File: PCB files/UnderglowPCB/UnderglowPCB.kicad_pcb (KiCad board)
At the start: 4 copper layers, 67 parts, among them J1 USB_B_Micro, J10 Screw_Terminal_01x03, J11 Screw_Terminal_01x03, J12 DB9_Male, J2 Screw_Terminal_01x03, J3 Screw_Terminal_01x03, J4 Conn_01x07, J5 Conn_01x05, J6 Screw_Terminal_01x03, J7 Screw_Terminal_01x03, J8 Screw_Terminal_01x03, J9 Screw_Terminal_01x03, Q1 S8050, Q2 S8050, SW1 SW_Push, U1 CP2102N-A01-GQFN28, U2 TPS62133, U3 74HC14, U4 74HC14, U5 LD56100DPU33R, U6 ESP32-WROOM-32D, U7 SN65HVD230, U8 USBLC6-2SC6

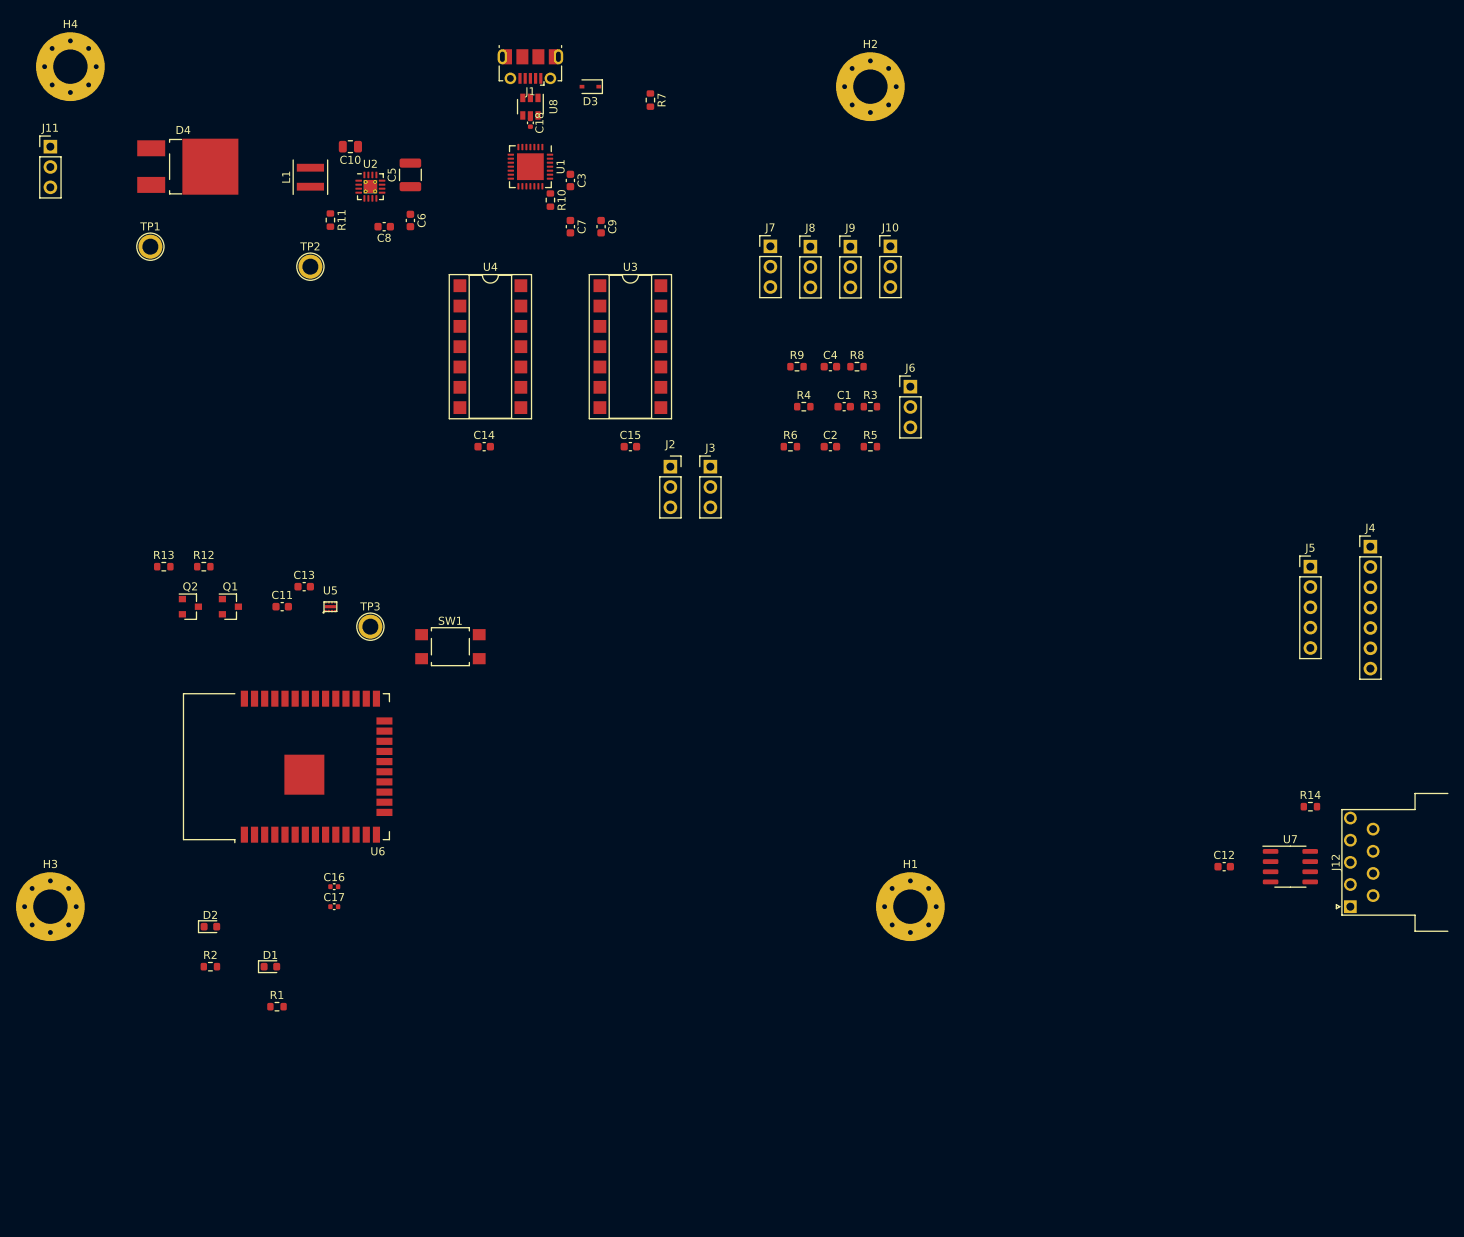
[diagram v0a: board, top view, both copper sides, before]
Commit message: Version 1.0.0 of PCB is almost done. Need tooling holes and holds for DB9 mount.
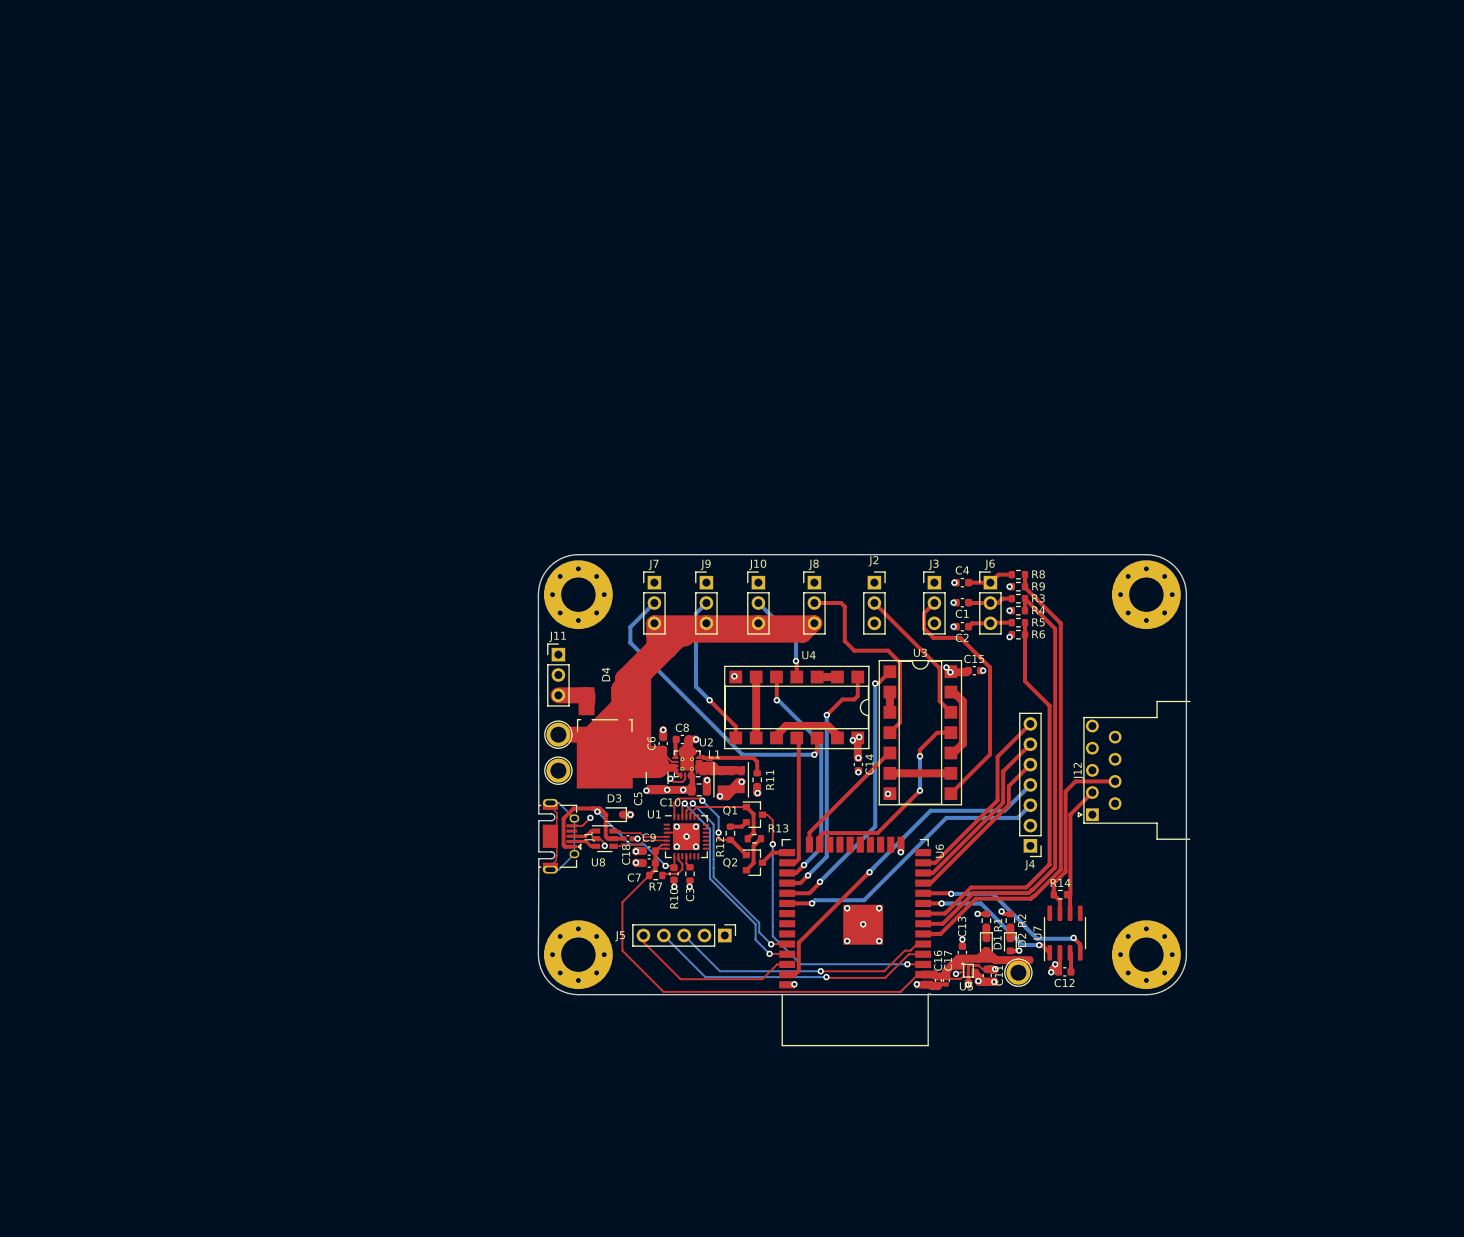
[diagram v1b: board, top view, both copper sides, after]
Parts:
- removed SW1: SW_Push, Button_Switch_SMD:SW_SPST_TL3305A
- J1: footprint Connector_USB:USB_Micro-B_Molex-105017-0001 -> Connector_USB:USB_Micro-AB_Molex_47590-0001
- moved R2 100.2 mm to (160.0, 126.8), turned to 90 degrees
- moved D2 100.0 mm to (160.0, 129.8), turned to 270 degrees
- moved C11 99.5 mm to (157.1, 133.6), turned to 90 degrees
- moved R7 96.9 mm to (115.7, 121.1), turned to 180 degrees
- moved J1 96.2 mm to (102.5, 116.2), turned to 270 degrees
- moved C13 94.1 mm to (154.0, 130.7), turned to 90 degrees
- moved U8 92.0 mm to (109.3, 116.5), turned to 0 degrees
- moved L1 91.9 mm to (125.1, 109.2), turned to 270 degrees
- moved TP3 91.8 mm to (161.0, 133.2), turned to 270 degrees
- moved U5 91.8 mm to (154.8, 133.0), turned to 270 degrees
- moved H4 91.6 mm to (106.0, 86.0)
- moved C10 91.5 mm to (121.1, 110.4), turned to 0 degrees
- moved D3 91.0 mm to (110.5, 113.5)
- moved C18 90.3 mm to (112.2, 116.5), turned to 0 degrees
- moved J11 89.8 mm to (103.5, 93.5)
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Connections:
- C5 pad 1: Net-(C5-Pad1) -> +12V
- C6 pad 1: Net-(C5-Pad1) -> +12V
- D4 pad 1: Net-(C5-Pad1) -> +12V
- D4 pad 2: +12V -> CAR_12V
- J11 pad 1: +12V -> GND
- J11 pad 3: GND -> CAR_12V
- J4 pad 2: +3V3 -> +5V
- U2 pad 10: Net-(C5-Pad1) -> +12V
- U2 pad 11: Net-(C5-Pad1) -> +12V
- U2 pad 12: Net-(C5-Pad1) -> +12V
- U2 pad 13: Net-(C5-Pad1) -> +12V
- U6 pad 10: UG_LOW_RIGHT -> CAN_RX
- U6 pad 11: UG_LOW_REAR -> OLED_RESET
- U6 pad 12: UG_LOW_FRONT -> OLED_DC
- U6 pad 13: UG_LOW_SPARE_1 -> OLED_CS
- U6 pad 14: RELAY_OUT -> Net-(U6-Pad14)
- U6 pad 16: UG_LOW_LEFT -> Net-(U6-Pad16)
- U6 pad 24: OLED_CS -> UG_LOW_SPARE_1
- U6 pad 26: OLED_DC -> UG_LOW_FRONT
- U6 pad 27: CAN_TX -> UG_LOW_REAR
- U6 pad 28: CAN_RX -> UG_LOW_RIGHT
- U6 pad 29: OLED_RESET -> UG_LOW_LEFT
- U6 pad 33: JOYSTICK_B -> Net-(U6-Pad33)
- U6 pad 36: Net-(SW1-Pad1) -> JOYSTICK_B
- U6 pad 4: Net-(U6-Pad4) -> JOYSTICK_Y
- U6 pad 5: BRAKE_LOW -> JOYSTICK_X
- U6 pad 6: TURN_RIGHT_LOW -> BRAKE_LOW
- U6 pad 7: TURN_LEFT_LOW -> TURN_RIGHT_LOW
- U6 pad 8: JOYSTICK_X -> TURN_LEFT_LOW
- U6 pad 9: JOYSTICK_Y -> CAN_TX
- U8 pad 1: USB_D- -> USB_D+
- U8 pad 3: USB_D+ -> USB_D-
- U8 pad 4: D+ -> D-
- U8 pad 6: D- -> D+
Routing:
- net +12V: track 0.00 -> 144.0 mm
- net +3V3: track 0.00 -> 89.7 mm
- net BRAKE_LOW: track 0.00 -> 59.3 mm
- net TURN_RIGHT_LOW: track 0.00 -> 56.1 mm
- net GND: track 0.00 -> 54.6 mm, vias 0 -> 42
- net TURN_LEFT_LOW: track 0.00 -> 51.4 mm
- net MOSI: track 0.00 -> 42.8 mm, vias 0 -> 1
- net UNDRGLW_FRNT: track 0.00 -> 37.2 mm, vias 0 -> 1
- net EN: track 0.00 -> 36.3 mm, vias 0 -> 2
- net JOYSTICK_Y: track 0.00 -> 35.8 mm, vias 0 -> 1
- net SPICLK: track 0.00 -> 35.5 mm, vias 0 -> 1
- net UG_LOW_LEFT: track 0.00 -> 34.9 mm, vias 0 -> 2
- net JOYSTICK_X: track 0.00 -> 33.1 mm, vias 0 -> 1
- net VBUS: track 0.00 -> 32.5 mm, vias 0 -> 2
- net 5V_LED_SPARE_2: track 0.00 -> 31.8 mm
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- added copper zone on In2.Cu, net +5V
- added copper zone on In1.Cu, net GND
- added copper zone on F.Cu, net Net-(L1-Pad1)
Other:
- board outline added: 81 x 55 mm
- net class Default: clearance 0.2 -> 0.1; trace_width 0.25 -> 0.4
- rule trace_clearance: 0.2 -> 0.1
- rule trace_min: 0.2 -> 0.15

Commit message: Minor PCB updates
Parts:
- added REF**: Pin_D1.0mm_L10.0mm, Connector_Pin:Pin_D1.0mm_L10.0mm, F.Cu at (109.8, 91.2)
- J12: footprint Connector_Dsub:DSUB-9_Male_Horizontal_P2.77x2.84mm_EdgePinOffset9.40mm -> UnderglowPCB:DB9
- moved J12 6.15 mm to (173.0, 108.0)
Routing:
- net GND: track 54.6 -> 74.8 mm
- net +5V: track 31.6 -> 40.8 mm
- net +3V3: track 89.7 -> 98.8 mm
- net Net-(J12-Pad7): track 22.9 -> 24.2 mm
- net Net-(J12-Pad2): track 16.8 -> 18.1 mm
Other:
- board text added: "+"
- board text added: "+3.3V"
- board text added: "+5V"
- board text added: "12V TEST POINT"
- board text added: "3.3V TEST POINT"
- board text added: "5V TEST POINT"
- board text added: "CAN BUS"
- board text added: "FRONT"
- board text added: "JOYSTICK"
- board text added: "LEFT"
- board text added: "REAR"
- board text added: "RIGHT"
- board text added: "SCREEN"
- board text added: "SPARE 1"
- board text added: "SPARE 2"
- board text added: "USB"

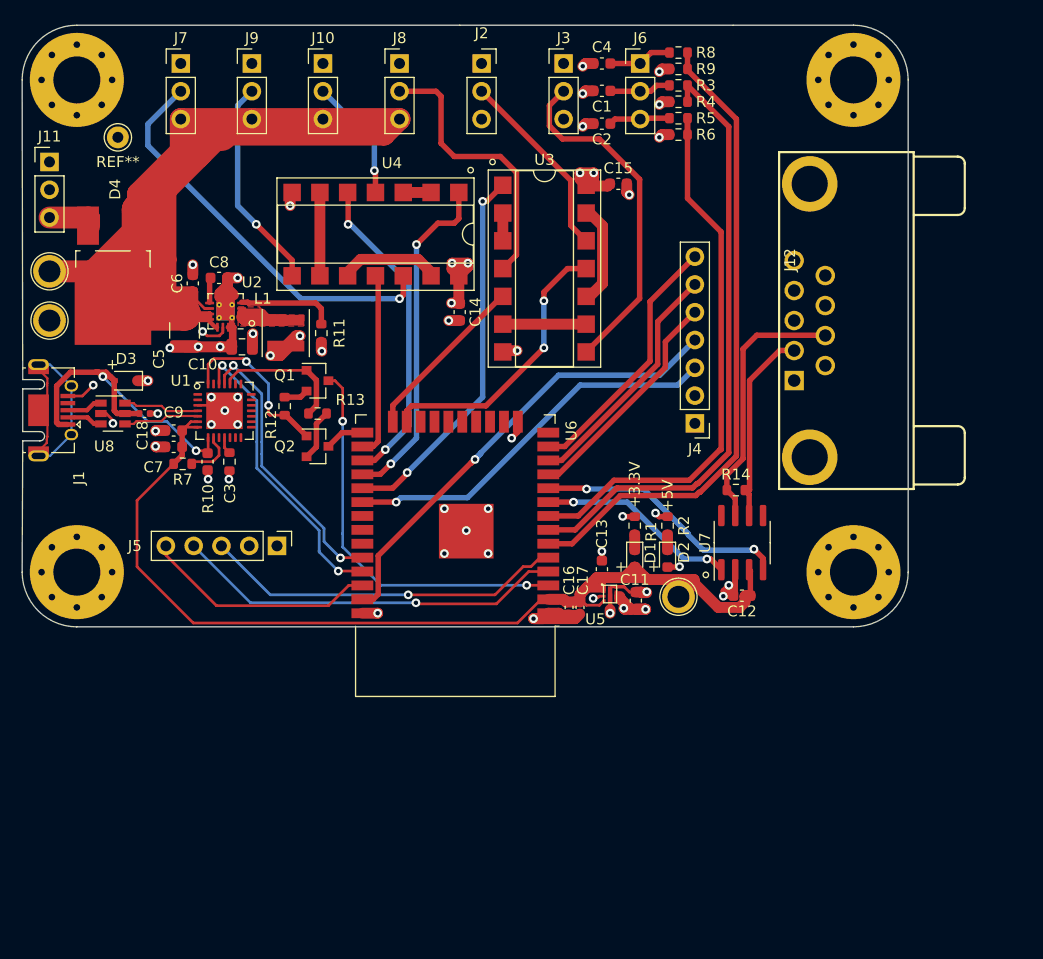
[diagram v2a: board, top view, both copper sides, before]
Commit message: Posted to reddit, changes include TVS Zener diodes and new power solution. That's a lot bigger.
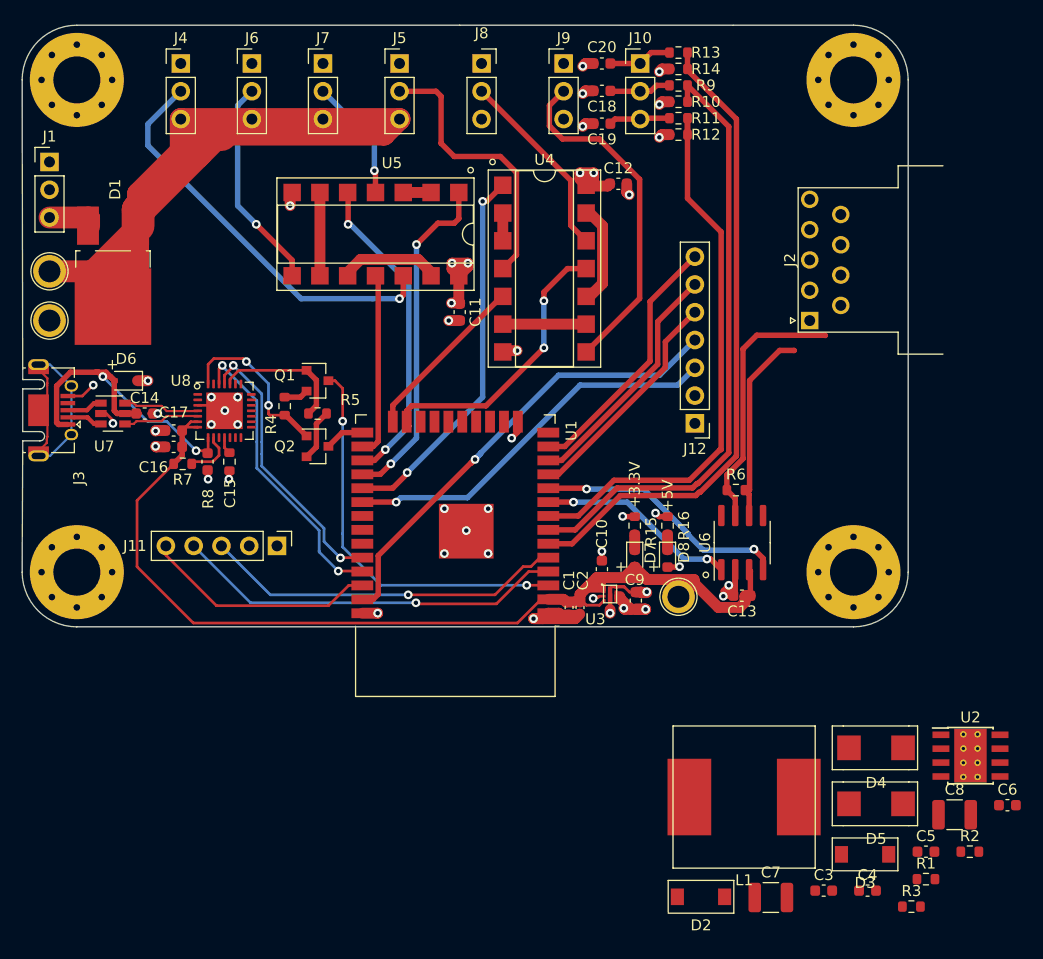
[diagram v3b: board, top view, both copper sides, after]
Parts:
- removed the C10 at (121.1, 110.4)
- removed the C18 at (112.2, 116.5)
- removed the J12 at (173.0, 108.0)
- removed the R11 at (128.3, 109.2)
- removed REF**: Pin_D1.0mm_L10.0mm, Connector_Pin:Pin_D1.0mm_L10.0mm
- added C14: .1u, Capacitor_SMD:C_0603_1608Metric, F.Cu at (112.2, 116.5)
- added C3: 2.2u, Capacitor_SMD:C_0603_1608Metric, F.Cu at (174.3, 160.1)
- added C4: 2.2u, Capacitor_SMD:C_0603_1608Metric, F.Cu at (178.3, 160.1)
- added C7: 47u, Capacitor_SMD:C_1210_3225Metric, F.Cu at (169.4, 160.7)
- added D2: TPSMA6L15A, UnderglowPCB:TPSMA6L15A, F.Cu at (163.1, 160.7)
- added D3: VSSAF512, UnderglowPCB:TPSMA6L15A, F.Cu at (178.1, 156.8)
- added D4: TPSMB15CA, UnderglowPCB:TPSMB15CA, F.Cu at (179.1, 147.1)
- added D5: TPSMB15CA, UnderglowPCB:TPSMB15CA, F.Cu at (179.1, 152.2)
- added J2: DB9_Male, Connector_Dsub:DSUB-9_Male_Horizontal_P2.77x2.84mm_EdgePinOffset9.40mm, F.Cu at (173.0, 108.0)
- added R1: 49.9k, Resistor_SMD:R_0603_1608Metric, F.Cu at (183.6, 159.1)
- added R2: 100k, Resistor_SMD:R_0603_1608Metric, F.Cu at (187.6, 156.6)
- added R3: 17.8k, Resistor_SMD:R_0603_1608Metric, F.Cu at (182.3, 161.6)
- C5: value 10u -> 22n; footprint Capacitor_SMD:C_1210_3225Metric -> Capacitor_SMD:C_0603_1608Metric
- C6: value 0.1u -> .1u
- C8: value 3.3n -> 47u; footprint Capacitor_SMD:C_0603_1608Metric -> Capacitor_SMD:C_1210_3225Metric
- L1: value 2.2u -> SRR1208-6R5ML; footprint Inductor_SMD:L_Coilcraft_XxL4020 -> UnderglowPCB:SRR1208
- U2: value TPS62133 -> LMR14030-Q1; footprint Package_DFN_QFN:VQFN-16-1EP_3x3mm_P0.5mm_EP1.68x1.68mm_ThermalVias -> Package_SO:Texas_HSOP-8-1EP_3.9x4.9mm_P1.27mm_ThermalVias
- moved C6 88.4 mm to (191.1, 152.3), turned to 0 degrees
- moved C8 83.2 mm to (186.2, 153.2)
- moved C5 82.9 mm to (183.6, 156.6), turned to 0 degrees
- moved U2 79.3 mm to (187.7, 147.8), turned to 0 degrees
- moved L1 59.6 mm to (167.0, 151.6), turned to 0 degrees
- renumbered C16 to C1, C13 to C10, C14 to C11, C15 to C12, C12 to C13, C3 to C15, C7 to C16, C9 to C17, C1 to C18, C2 to C19, C17 to C2, C4 to C20, C11 to C9, D4 to D1, D3 to D6, D1 to D7, D2 to D8, J11 to J1, J6 to J10, J5 to J11, J4 to J12, J1 to J3, J7 to J4, J8 to J5, J9 to J6, J10 to J7, J2 to J8, J3 to J9, R4 to R10, R5 to R11, R6 to R12, R8 to R13, R9 to R14, R1 to R15, R2 to R16, R12 to R4, R13 to R5, R14 to R6, R10 to R8, R3 to R9, U6 to U1, U5 to U3, U3 to U4, U4 to U5, U7 to U6, U8 to U7, U1 to U8
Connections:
- net RELAY_OUT renamed Net-(J1-Pad2)
- C5 pad 1: +12V -> Net-(C5-Pad1)
- C6 pad 1: +12V -> Net-(C6-Pad1)
- C6 pad 2: GND -> Net-(C6-Pad2)
- C8 pad 1: Net-(C8-Pad1) -> +5V
- L1 pad 1: Net-(L1-Pad1) -> Net-(C6-Pad2)
- U2 pad 1: Net-(L1-Pad1) -> Net-(C6-Pad1)
- U2 pad 2: Net-(L1-Pad1) -> +12V
- U2 pad 3: Net-(L1-Pad1) -> Net-(U2-Pad3)
- U2 pad 5: GND -> Net-(R2-Pad2)
- U2 pad 6: GND -> Net-(C5-Pad1)
- U2 pad 8: GND -> Net-(C6-Pad2)
- U2 pad 9: Net-(C8-Pad1) -> (no net)
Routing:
- net +12V: track 144.0 -> 100.0 mm
- net GND: track 74.8 -> 53.3 mm, vias 42 -> 37
- net Net-(L1-Pad1): track 15.9 -> 0.00 mm
- net +5V: track 40.8 -> 31.0 mm, vias 15 -> 10
- net Net-(R1-Pad1): track 8.95 -> 0.00 mm
- net Net-(C8-Pad1): track 2.26 -> 0.00 mm
- removed copper zone on F.Cu, net Net-(L1-Pad1)

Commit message: Lastest draft of device
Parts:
- removed TP1, TP2, TP3: TestPoint, TestPoint:TestPoint_Plated_Hole_D2.0mm
- added F1: 3413.0330.22, Fuse:Fuse_1206_3216Metric, F.Cu at (91.2, 64.5)
- C10, C9: value 2.2u -> 10u
- J2: footprint Connector_Dsub:DSUB-9_Male_Horizontal_P2.77x2.84mm_EdgePinOffset9.40mm -> UnderglowPCB:DB9
- U3: value LD56100DPU33R -> NCP1117-3.3_SOT223; footprint UnderglowPCB:LD56100DPU33R -> Package_TO_SOT_SMD:SOT-223-3_TabPin2
- moved D2 124.9 mm to (89.8, 59.5), turned to 90 degrees
- moved R1 123.9 mm to (102.2, 65.6), turned to 270 degrees
- moved C6 122.0 mm to (108.5, 62.6)
- moved C4 121.9 mm to (107.2, 61.0)
- moved C3 121.0 mm to (107.2, 59.4)
- moved R3 117.2 mm to (104.8, 73.6)
- moved R2 116.1 mm to (104.0, 76.0), turned to 90 degrees
- moved C5 114.9 mm to (105.8, 72.0)
- moved U2 114.7 mm to (105.8, 67.4), turned to 270 degrees
- moved D3 109.9 mm to (110.5, 70.2), turned to 90 degrees
- moved H1 109.1 mm to (69.8, 111.0)
- moved C7 94.4 mm to (128.7, 75.6)
- moved C8 93.9 mm to (128.7, 79.0)
- moved L1 88.3 mm to (119.0, 77.4)
- moved D5 86.2 mm to (155.8, 69.2), turned to 270 degrees
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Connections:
- D1 pad 2: CAR_12V -> Net-(D1-Pad2)
- D2 pad 1: +12V -> CAR_12V
- J11 pad 2: +5V -> +3V3
- U2 pad 9: (no net) -> GND
- U3 pad 1: +3V3 -> GND
- U4 pad 1: UG_LOW_LEFT -> UG_LOW_RIGHT
- U4 pad 10: Net-(U4-Pad10) -> 5V_LED_SPARE_1
- U4 pad 11: UG_LOW_SPARE_2 -> Net-(U4-Pad11)
- U4 pad 12: 5V_LED_SPARE_1 -> UNDRGLW_RGHT
- U4 pad 13: Net-(U4-Pad10) -> Net-(U4-Pad13)
- U4 pad 2: Net-(U4-Pad2) -> Net-(U4-Pad13)
- U4 pad 3: Net-(U4-Pad2) -> UG_LOW_SPARE_2
- U4 pad 4: UNDRGLW_LEFT -> Net-(U4-Pad11)
- U5 pad 1: UG_LOW_RIGHT -> UG_LOW_FRONT
- U5 pad 10: Net-(U5-Pad10) -> UNDRGLW_LEFT
- U5 pad 11: UG_LOW_FRONT -> Net-(U5-Pad11)
- U5 pad 13: Net-(U5-Pad10) -> Net-(U5-Pad13)
- U5 pad 2: Net-(U5-Pad2) -> Net-(U5-Pad13)
- U5 pad 3: Net-(U5-Pad2) -> UG_LOW_LEFT
- U5 pad 4: UNDRGLW_RGHT -> Net-(U5-Pad11)
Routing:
- net +12V: track 100.0 -> 0.00 mm
- net +3V3: track 98.8 -> 9.12 mm
- net BRAKE_LOW: track 59.3 -> 1.50 mm
- net TURN_RIGHT_LOW: track 56.1 -> 1.50 mm
- net TURN_LEFT_LOW: track 51.4 -> 1.50 mm
- net MOSI: track 42.8 -> 0.00 mm, vias 1 -> 0
- net UNDRGLW_FRNT: track 37.2 -> 0.00 mm, vias 1 -> 0
- net EN: track 36.3 -> 0.00 mm, vias 2 -> 0
- net JOYSTICK_Y: track 35.8 -> 0.00 mm, vias 1 -> 0
- net SPICLK: track 35.5 -> 0.00 mm, vias 1 -> 0
- net UG_LOW_LEFT: track 34.9 -> 0.00 mm, vias 2 -> 0
- net JOYSTICK_X: track 33.1 -> 0.00 mm, vias 1 -> 0
- net 5V_LED_SPARE_2: track 31.8 -> 0.00 mm
- net UG_LOW_RIGHT: track 31.3 -> 0.00 mm, vias 2 -> 0
- net UG_LOW_REAR: track 29.3 -> 0.00 mm, vias 2 -> 0
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- added copper zone on F.Cu, net Net-(C6-Pad2)
- removed copper zone on In2.Cu, net +5V
- removed copper zone on In1.Cu, net GND
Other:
- board size 81 x 55 mm -> 2 x 7.5 mm
